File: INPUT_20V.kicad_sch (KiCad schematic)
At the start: 5 parts

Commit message: improved analogs
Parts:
- R20: renamed from R23; value 1k -> 10k
- R21: renamed from R24; value 1.5k -> 1k
- renumbered C45 to C44, D4 to D3, R22 to R19
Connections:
- net INPUT renamed RAW
- net OUTPUT renamed IO

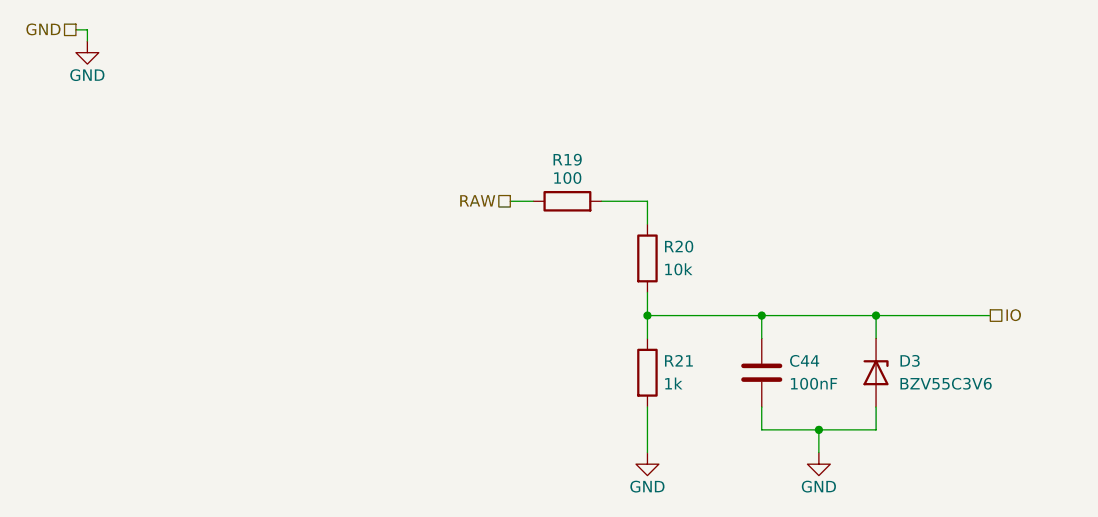
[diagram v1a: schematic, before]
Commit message: redid annotations, added test point
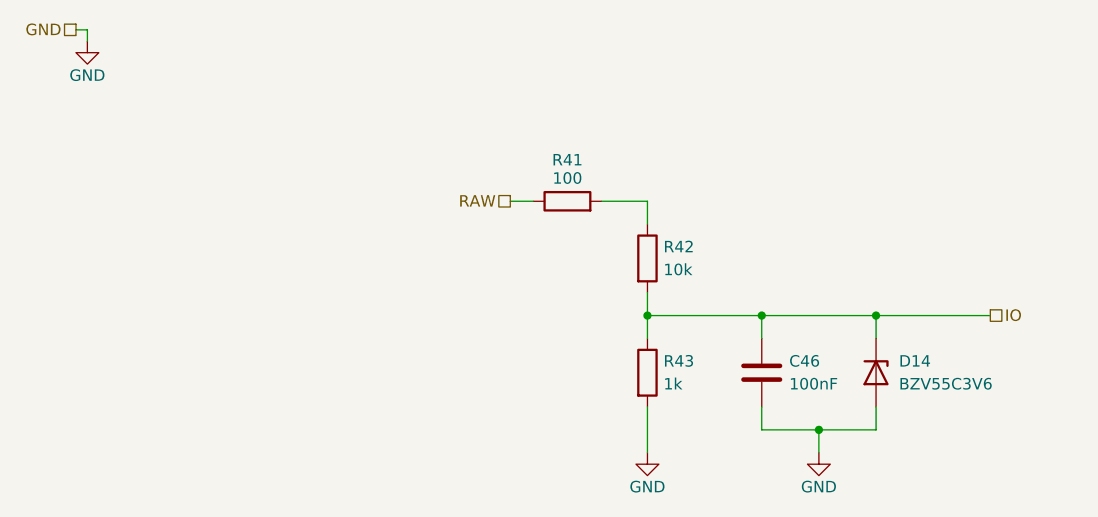
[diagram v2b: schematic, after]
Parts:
- renumbered C44 to C46, D3 to D14, R19 to R41, R20 to R42, R21 to R43
